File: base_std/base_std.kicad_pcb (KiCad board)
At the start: 2 copper layers, 25.2 x 30 mm, 25 parts, among them J1 Moat_Wire_12, J10 1wireConn, J2 Moat_Bus_wire, J3 I2C, J4 Conn_01x08, Q1 2N7002, Q2 2N7002, Q3 2N7002, Q4 2N7002, U1 MIC5504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

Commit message: proc_stm32
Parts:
- added REF**: OSHW-Logo_5.7x6mm_Copper, Symbol:OSHW-Logo_5.7x6mm_Copper, B.Cu at (31.2, 35.2)
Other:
- board text added: "JLCJLCJLCJLC"
- board text added: "MoaT Base v1.0"

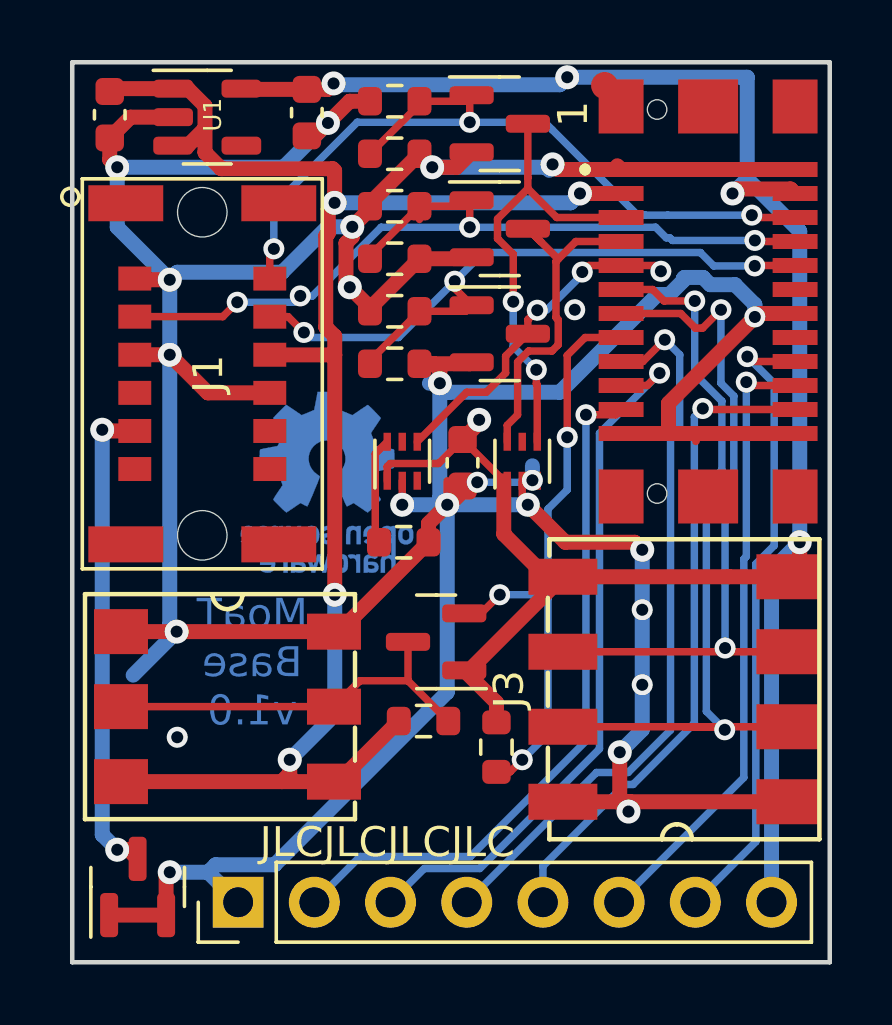
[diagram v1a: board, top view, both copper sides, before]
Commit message: Plug updates
drop in/out from plug24
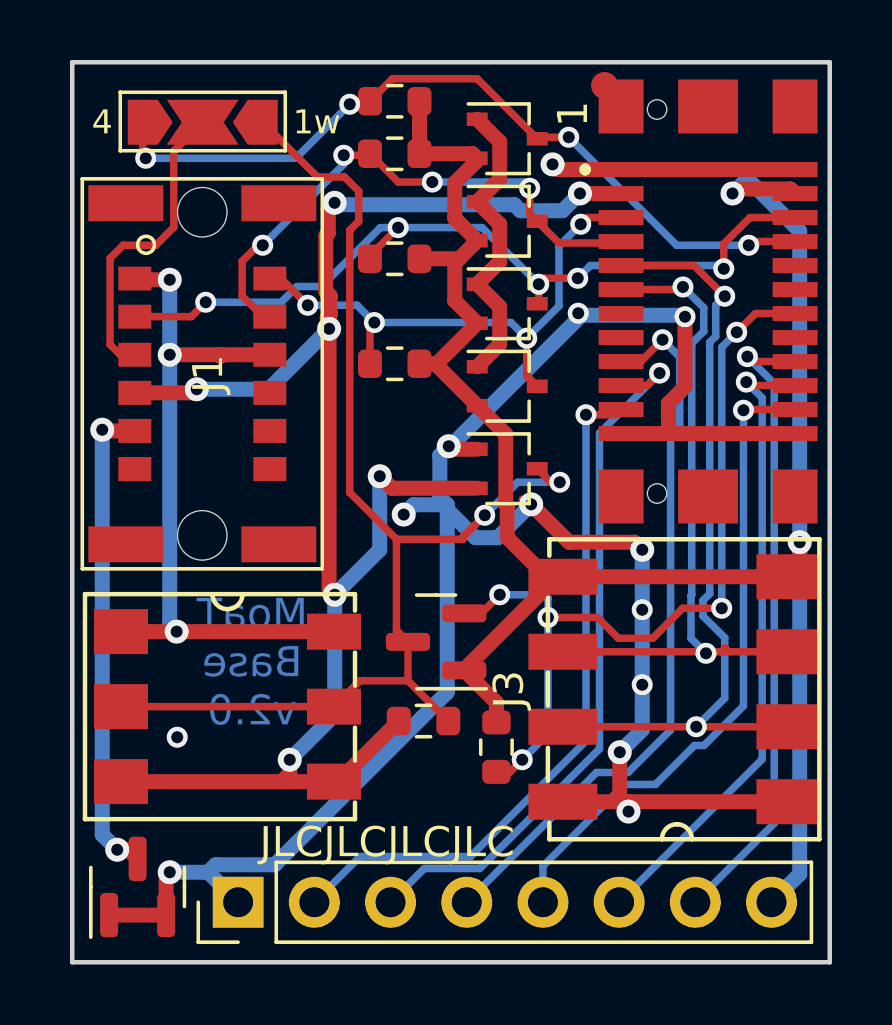
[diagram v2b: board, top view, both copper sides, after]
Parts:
- removed C1, C2: 1µ, Capacitor_SMD:C_0603_1608Metric
- removed C3: 100n, Capacitor_SMD:C_0603_1608Metric
- removed Q2, Q3, Q4: 2N7002, Package_TO_SOT_SMD:SOT-23
- removed R4, R8: 1M, Resistor_SMD:R_0603_1608Metric
- removed R9: 10k, Resistor_SMD:R_0603_1608Metric
- removed REF**: OSHW-Logo_5.7x6mm_Copper, Symbol:OSHW-Logo_5.7x6mm_Copper
- removed U1: MIC5504, Package_TO_SOT_SMD:SOT-23-5
- removed U2, U3: LTC4311, Package_DFN_QFN:ST_UQFN-6L_1.5x1.7mm_Pitch0.5mm
- added D2: BAT54SW, Package_TO_SOT_SMD:SOT-323_SC-70, F.Cu at (37.2, 32.0)
- added D3: BAT54SW, Package_TO_SOT_SMD:SOT-323_SC-70, F.Cu at (37.2, 29.2)
- added D4: BAT54SW, Package_TO_SOT_SMD:SOT-323_SC-70, F.Cu at (37.2, 26.5)
- added D5: BAT54SW, Package_TO_SOT_SMD:SOT-323_SC-70, F.Cu at (37.2, 23.8)
- added D6: BAT54SW, Package_TO_SOT_SMD:SOT-323_SC-70, F.Cu at (37.2, 34.8)
- added JP1: SolderJumper_3_Open, Jumper:SolderJumper-3_P2.0mm_Open_TrianglePad1.0x1.5mm_NumberLabels, F.Cu at (27.1, 23.2)
- R3: value 1M -> 470
- turned R3 to 0 degrees
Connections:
- J1 pad 2: /Bus1_out -> /Bus1
- J1 pad 3: /Bus2_out -> /Bus2
- J1 pad 4: /Bus3_out -> /Bus3
- J1 pad 5: GND -> /Bus4W
- J1 pad 6: +5V -> GND
- J1 pad 7: +12V -> +5V
- J1 pad 8: GND -> +12V
- J2 pad 10: /Bus3_out -> unconnected-(J2-Pad10)
- J2 pad 13: Net-(J2-Pad13) -> unconnected-(J2-Pad13)
- J2 pad 14: GND -> /1wire_3
- J2 pad 15: /1wire_3 -> unconnected-(J2-Pad15)
- J2 pad 24: GND -> unconnected-(J2-Pad24)
- J2 pad 5: /Bus1_in -> /Bus1
- J2 pad 6: /Bus1_out -> /Bus2
- J2 pad 7: /Bus2_in -> /Bus3
- J2 pad 8: /Bus2_out -> /Bus4
- J2 pad 9: /Bus3_in -> Net-(J2-Pad9)
- J3 pad 2: Net-(J2-Pad11) -> Net-(J2-Pad9)
- J3 pad 3: Net-(J2-Pad13) -> Net-(J2-Pad11)
- R3 pad 1: /Bus1_out -> /Bus4
- R3 pad 2: GND -> +3V3
- R5 pad 1: /Bus2_out -> /Bus2
- R5 pad 2: GND -> +3V3
- R6 pad 1: /Bus3_out -> /Bus1
- R6 pad 2: GND -> +3V3
- R7 pad 1: /Bus1_out -> /Bus3
- R7 pad 2: GND -> +3V3
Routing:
- net GND: track 170.6 -> 114.4 mm, vias 24 -> 16
- net /Bus2_out: track 29.1 -> 0.00 mm, vias 4 -> 0
- net /Bus1_out: track 28.0 -> 0.00 mm, vias 3 -> 0
- net /Bus2: track 0.00 -> 27.5 mm, vias 0 -> 5
- net /1wire_5: track 13.2 -> 40.6 mm, vias 0 -> 2
- net Net-(J2-Pad9): track 0.00 -> 26.7 mm, vias 0 -> 2
- net /Bus4: track 0.00 -> 26.4 mm, vias 0 -> 4
- net /Bus3_out: track 24.6 -> 0.00 mm, vias 3 -> 0
- net Net-(J2-Pad13): track 23.0 -> 0.00 mm, vias 2 -> 0
- net /Bus1: track 0.00 -> 18.6 mm, vias 0 -> 4
- net /Bus3: track 0.00 -> 18.4 mm, vias 0 -> 4
- net /Bus1_in: track 15.1 -> 0.00 mm, vias 2 -> 0
- net /Bus2_in: track 11.7 -> 0.00 mm
- net /Bus3_in: track 11.1 -> 0.00 mm, vias 3 -> 0
- net /Bus4W: track 0.00 -> 10.3 mm
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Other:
- board text added: "MoaT Base v2.0"
- board text removed: "MoaT Base v1.0"

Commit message: No save for too long …
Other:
- board text removed: "JLCJLCJLCJLC"
